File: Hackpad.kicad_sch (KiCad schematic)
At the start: 5 parts, among them SW1 SW_Push, SW2 SW_Push, SW3 SW_Push, SW4 SW_Push, U1 MOUDLE-SEEEDUINO-XIAO

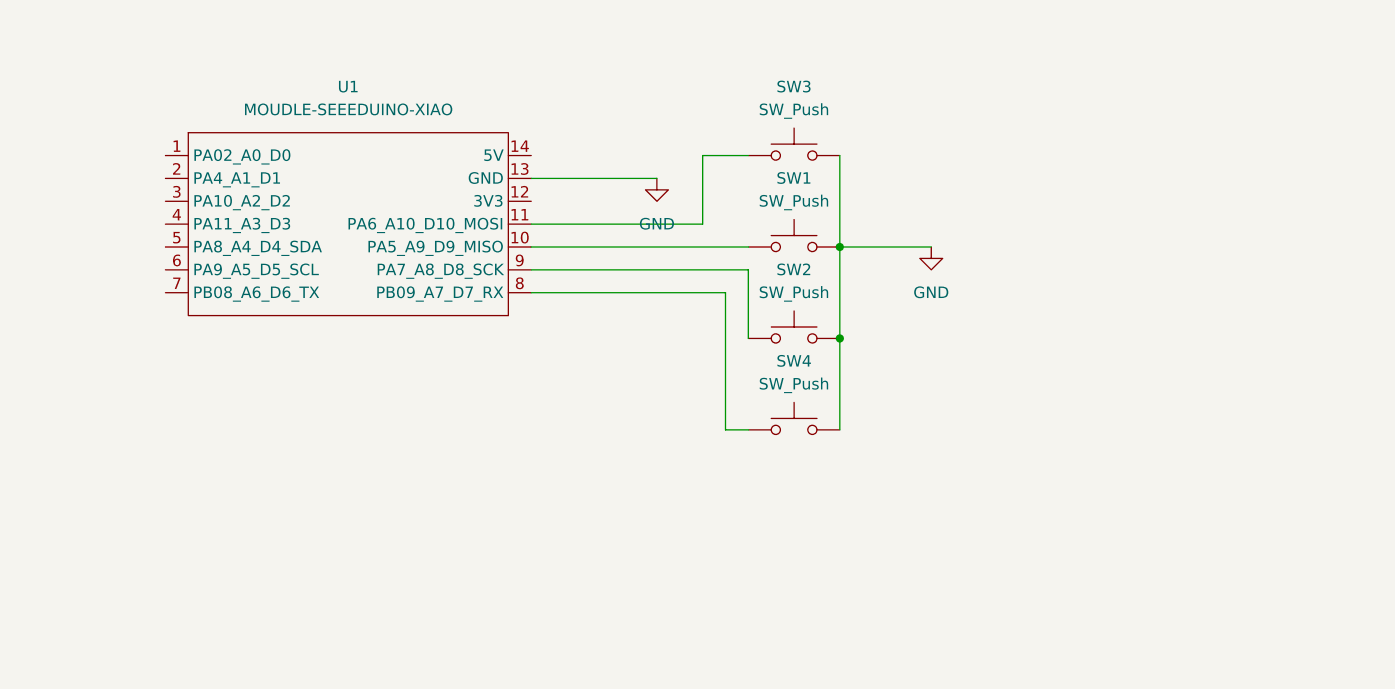
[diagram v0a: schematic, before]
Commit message: Make schematic
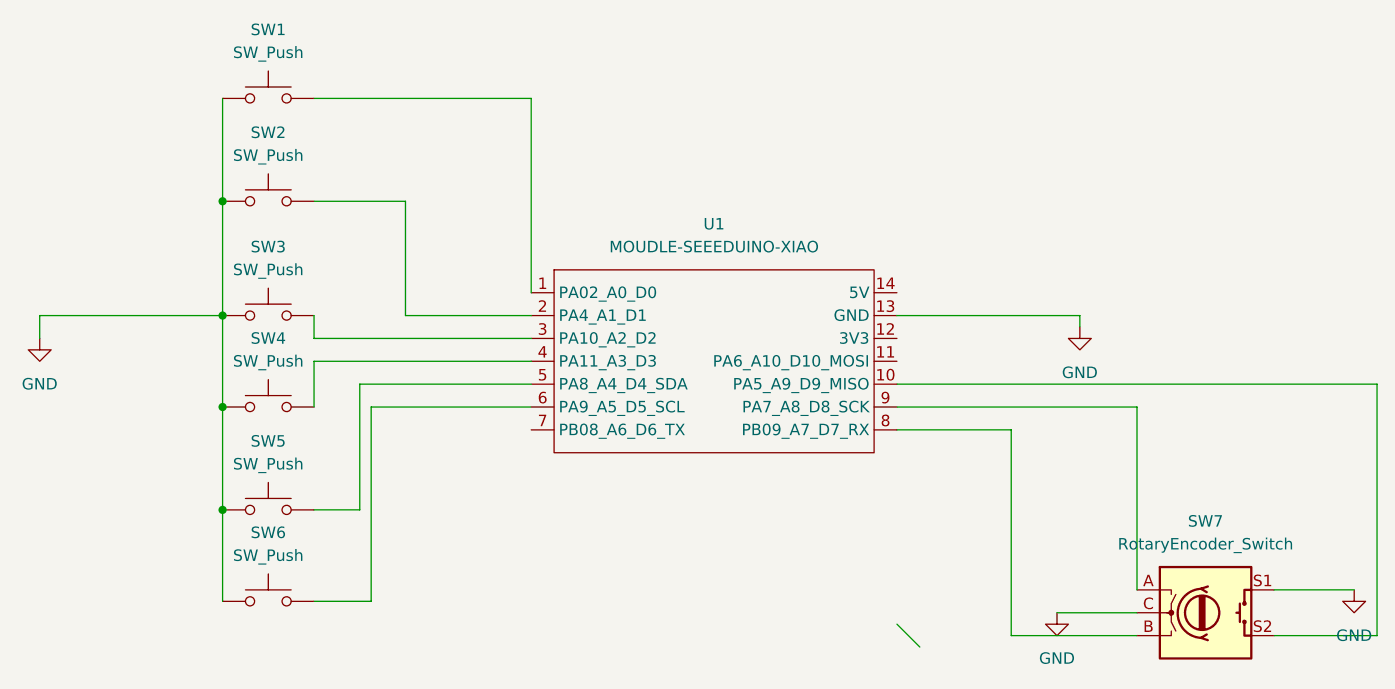
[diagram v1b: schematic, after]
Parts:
- added SW5, SW6: SW_Push, symbol Switch:SW_Push
- added SW7: RotaryEncoder_Switch, Oscillator:Oscillator_SMD_ECS_2520MV-xxx-xx-4Pin_2.5x2.0mm, symbol Device:RotaryEncoder_Switch
- SW1, SW2, SW3: footprint Button_Switch_Keyboard:SW_Cherry_MX_1.00u_PCB -> (none)
- U1: footprint footprints:XIAO-Generic-Hybrid-14P-2.54-21X17.8MM -> Package_QFP:TQFP-44_10x10mm_P0.8mm
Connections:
- net GND: now also SW1.1, SW2.1, SW3.1, SW4.1, SW5.1, SW6.1, SW7.C, SW7.S1; no longer SW1.2, SW2.2, SW3.2, SW4.2
- net at U1.1 (PA02_A0_D0): now also SW1.2
- net at U1.10 (PA5_A9_D9_MISO): now also SW7.S2; no longer SW1.1
- net at U1.11 (PA6_A10_D10_MOSI): no longer SW3.1
- net at U1.2 (PA4_A1_D1): now also SW2.2
- net at U1.3 (PA10_A2_D2): now also SW3.2
- net at U1.4 (PA11_A3_D3): now also SW4.2
- net at U1.5 (PA8_A4_D4_SDA): now also SW5.2
- net at U1.6 (PA9_A5_D5_SCL): now also SW6.2
- net at U1.8 (PB09_A7_D7_RX): now also SW7.B; no longer SW4.1
- net at U1.9 (PA7_A8_D8_SCK): now also SW7.A; no longer SW2.1
